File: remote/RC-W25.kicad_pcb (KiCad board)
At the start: 2 copper layers, 36 x 100.1 mm, 56 parts, among them J1 USB_C_Receptacle_USB2.0_14P, P1 JST CONN, P2 JST CONN, Q1 NMOS, SW1 Button, SW2 Button, SW3 YTSPS-22E58LM, SW4 Button, U1 ESP32-C6-MINI-1, U2 MCP73831-5-OT, U3 AP62300Z6, U4 TMAG5253

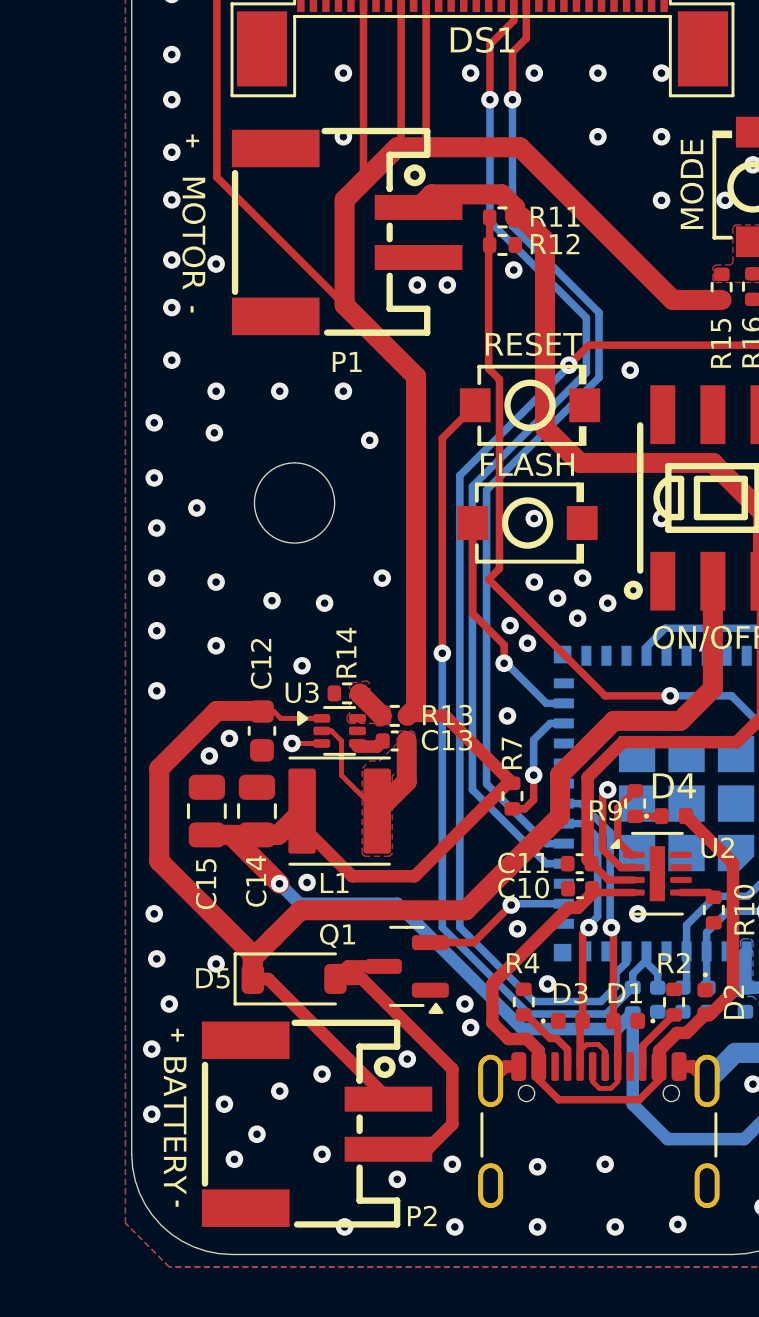
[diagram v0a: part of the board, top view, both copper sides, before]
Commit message: updated traces
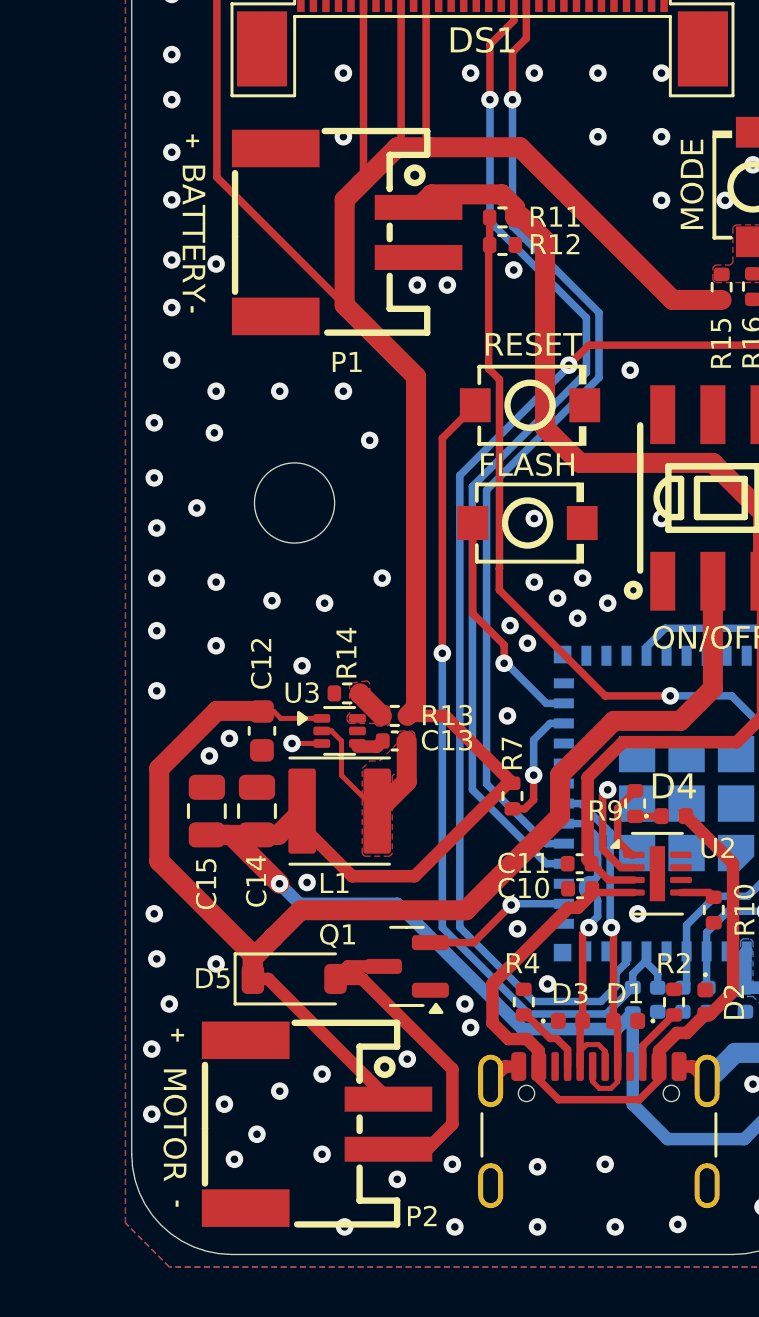
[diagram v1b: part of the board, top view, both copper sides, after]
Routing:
- net USB_D-: track 13.4 -> 14.2 mm
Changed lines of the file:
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@@
 		)
 	)
-	(gr_text "BATTERY"
+	(gr_text "MOTOR"
 		(at 112.7 119.8 270)
 		(layer "F.SilkS")
@@
 		)
 	)
-	(gr_text "MOTOR"
+	(gr_text "BATTERY"
 		(at 113.451866 84.206002 270)
 		(layer "F.SilkS")
@@
 	)
 	(segment
-		(start 129.9 102.7)
-		(end 125.25 98.05)
+		(start 125.675 97.625)
+		(end 125.68 97.62)
 		(width 0.3)
 		(layer "F.Cu")
@@
 	)
 	(segment
-		(start 132.5 102.7)
-		(end 129.9 102.7)
+		(start 125.25 84.74)
+		(end 125.29 84.7)
 		(width 0.3)
 		(layer "F.Cu")
@@
 	)
 	(segment
-		(start 125.25 84.74)
-		(end 125.29 84.7)
+		(start 125.68 90.07)
+		(end 125.25 89.64)
 		(width 0.3)
 		(layer "F.Cu")
@@
 	)
 	(segment
-		(start 125.68 90.07)
-		(end 125.25 89.64)
+		(start 125.68 97.62)
+		(end 125.68 90.07)
 		(width 0.3)
 		(layer "F.Cu")
@@
 	)
 	(segment
-		(start 125.25 98.05)
-		(end 125.68 97.62)
+		(start 132.5 102.7)
+		(end 129.9 102.7)
 		(width 0.3)
 		(layer "F.Cu")
@@
 	)
 	(segment
-		(start 125.68 97.62)
-		(end 125.68 90.07)
+		(start 129.9 102.7)
+		(end 125.675 98.475)
+		(width 0.3)
+		(layer "F.Cu")
+		(net 11)
+	)
+	(segment
+		(start 125.675 98.475)
+		(end 125.675 97.625)
 		(width 0.3)
 		(layer "F.Cu")
@@
 	)
 	(segment
-		(start 129.036093 107.8)
-		(end 128.25 107.8)
+		(start 129.25 111.949998)
+		(end 129.25 111.860051)
 		(width 0.3)
 		(layer "B.Cu")
@@
 	)
 	(segment
-		(start 129.25 111.949998)
-		(end 129.25 111.860051)
+		(start 129.36 110.654275)
+		(end 129.24 110.654275)
 		(width 0.3)
 		(layer "B.Cu")
@@
 	(segment
 		(start 129.6 111.510051)
-		(end 129.6 108.363907)
+		(end 129.6 110.894275)
+		(width 0.3)
+		(layer "B.Cu")
+		(net 19)
+	)
+	(segment
+		(start 129.036093 107.8)
+		(end 128.25 107.8)
 		(width 0.3)
 		(layer "B.Cu")
@@
 	)
 	(segment
+		(start 129.6 109.694275)
+		(end 129.6 109.553248)
+		(width 0.3)
+		(layer "B.Cu")
+		(net 19)
+	)
+	(segment
+		(start 129.6 109.553248)
+		(end 129.6 108.363907)
+		(width 0.3)
+		(layer "B.Cu")
+		(net 19)
+	)
+	(segment
+		(start 129.24 110.054275)
+		(end 129.36 110.054275)
+		(width 0.3)
+		(layer "B.Cu")
+		(net 19)
+	)
+	(segment
+		(start 129.6 109.814275)
+		(end 129.6 109.694275)
+		(width 0.3)
+		(layer "B.Cu")
+		(net 19)
+	)
+	(segment
+		(start 129 110.414275)
+		(end 129 110.294275)
+		(width 0.3)
+		(layer "B.Cu")
+		(net 19)
+	)
+	(arc
+		(start 129.36 110.054275)
+		(mid 129.529706 109.983981)
+		(end 129.6 109.814275)
+		(width 0.3)
+		(layer "B.Cu")
+		(net 19)
+	)
+	(arc
+		(start 129 110.294275)
+		(mid 129.070294 110.124569)
+		(end 129.24 110.054275)
+		(width 0.3)
+		(layer "B.Cu")
+		(net 19)
+	)
+	(arc
+		(start 129.6 110.894275)
+		(mid 129.529706 110.724569)
+		(end 129.36 110.654275)
+		(width 0.3)
+		(layer "B.Cu")
+		(net 19)
+	)
+	(arc
+		(start 129.24 110.654275)
+		(mid 129.070294 110.583981)
+		(end 129 110.414275)
+		(width 0.3)
+		(layer "B.Cu")
+		(net 19)
+	)
+	(segment
 		(start 132.14 107.51)
 		(end 132.15 107.5)
@@
 		)
 	)
+	(generated
+		(type tuning_pattern)
+		(name "Tuning Pattern")
+		(layer "B.Cu")
+		(base_line
+			(pts
+				(xy 129.6 110.894275) (xy 129.6 109.553248)
+			)
+		)
+		(corner_radius_percent 80)
+		(end
+			(xy 129.6 109.553248)
+		)
+		(initial_side "left")
+		(last_diff_pair_gap 0.18)
+		(last_netname "USB_D-")
+		(last_status "tuned")
+		(last_track_width 0.3)
+		(last_tuning "11.4774 mm (tuned)")
+		(max_amplitude 1)
+		(min_amplitude 0.2)
+		(min_spacing 0.6)
+		(origin
+			(xy 129.6 110.894275)
+		)
+		(override_custom_rules no)
+		(rounded yes)
+		(single_sided no)
+		(target_length 1000000)
+		(target_length_max 1000000)
+		(target_length_min 0)
+		(target_skew 0)
+		(target_skew_max 0.1)
+		(target_skew_min -0.1)
+		(tuning_mode "single")
+		(members "17cc8b51-adf3-4e6e-9451-abfa4a674d56" "2a80a1e3-7b09-4555-9cd4-e5b55d2daa5a"
+			"307ab3b6-0398-461d-9a12-6d7128e14987" "71b74942-a42e-4466-ac9a-01aa8737ae8c"
+			"856c1569-1c46-41f8-8312-75d96f11e951" "a7aceae7-cda2-42e2-861a-2e21ca846b52"
+			"bebe22a4-1710-4036-9746-54e66e6d4b58" "c35c4a82-8555-4b38-9e99-cf264392ba8c"
+			"dc328dce-c958-4ce4-8d3c-416cb03f53c3"
+		)
+	)

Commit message: CRC V3
V 3.0.0
Initial version of CRC V3, fully redesigned remote
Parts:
- removed G***: LOGO, LOGO
- removed H3: MountingHole, MountingHole:MountingHole_3.2mm_M3
- removed P1, P2: JST CONN, footprints:CONN-SMD_2P-P2.00_XUNPU_WAFER-PH2.0-2PWB
- removed SW1, SW2, SW4: Button, footprints:SW-SMD_L3.9-W3.0-P4.45
- removed SW3: YTSPS-22E58LM, footprints:SW-SMD_6P-YTSPS-22E58LM
- removed U4: TMAG5253, footprints:X2SON4_DMR_TEX
- added +3.3V: TEST POINT, TestPoint:TestPoint_Pad_2.0x2.0mm, F.Cu at (102.4, 126.1)
- added +USB5V: TEST POINT, TestPoint:TestPoint_Pad_2.0x2.0mm, F.Cu at (125.7, 129.5)
- added +VBAT: TEST POINT, TestPoint:TestPoint_Pad_2.0x2.0mm, F.Cu at (116.8, 122.0)
- added BATTERY: JST CONN, footprints:CONN-SMD_2P-P2.00_XUNPU_WAFER-PH2.0-2PWB, B.Cu at (120.6, 124.2)
- added BOOT: Button, footprints:SW-SMD_L3.9-W3.0-P4.45, F.Cu at (104.9, 100.5)
- added C18: 10uF, Capacitor_SMD:C_0402_1005Metric_Pad0.74x0.62mm_HandSolder, F.Cu at (121.0, 116.8)
- added C19: 100nF, Capacitor_SMD:C_0402_1005Metric_Pad0.74x0.62mm_HandSolder, F.Cu at (108.9, 121.0)
- added C20: 100nF, Capacitor_SMD:C_0402_1005Metric_Pad0.74x0.62mm_HandSolder, F.Cu at (107.9, 121.0)
- added D6: GLED, Diode_SMD:D_0402_1005Metric_Pad0.77x0.64mm_HandSolder, F.Cu at (105.7, 105.6)
- added D7: ZENER 5V, Diode_SMD:D_0402_1005Metric_Pad0.77x0.64mm_HandSolder, F.Cu at (118.9, 120.0)
- added D8: D_Schottky, Diode_SMD:D_SOD-123, F.Cu at (104.3, 93.5)
- added FB: TEST POINT, TestPoint:TestPoint_Pad_2.0x2.0mm, F.Cu at (113.5, 133.6)
- added JOYSTICK: TEST POINT, TestPoint:TestPoint_Pad_2.0x2.0mm, B.Cu at (114.6, 88.2)
- added JOYSTICK: JOYSTICK, footprints:Joystick Potentiometer Pads, B.Cu at (114.6, 84.0)
- added MODE: Button, footprints:Box Tactile Button Switch, F.Cu at (123.0, 102.0)
- added MOTOR: TEST POINT, TestPoint:TestPoint_Pad_2.0x2.0mm, F.Cu at (103.3, 90.2)
- added MOTOR: MOTOR, footprints:Motor Pads, B.Cu at (104.0, 91.5)
- added ON/OFF: Button, footprints:Box Tactile Button Switch, F.Cu at (123.0, 94.2)
- added R17: 1k, Resistor_SMD:R_0402_1005Metric_Pad0.72x0.64mm_HandSolder, F.Cu at (116.8, 119.2)
- added R18: 3.7k, Resistor_SMD:R_0402_1005Metric_Pad0.72x0.64mm_HandSolder, F.Cu at (116.8, 116.9)
- added R19: 1M, Resistor_SMD:R_0402_1005Metric_Pad0.72x0.64mm_HandSolder, F.Cu at (102.4, 123.8)
- added R20: 10k, Resistor_SMD:R_0402_1005Metric_Pad0.72x0.64mm_HandSolder, F.Cu at (117.6, 101.6)
- added R21: 10k, Resistor_SMD:R_0402_1005Metric_Pad0.72x0.64mm_HandSolder, F.Cu at (117.7, 93.8)
- added R22: 10k, Resistor_SMD:R_0402_1005Metric_Pad0.72x0.64mm_HandSolder, F.Cu at (118.2, 103.3)
- added R23: 10k, Resistor_SMD:R_0402_1005Metric_Pad0.72x0.64mm_HandSolder, F.Cu at (118.3, 95.5)
- added RESET: Button, footprints:SW-SMD_L3.9-W3.0-P4.45, F.Cu at (104.9, 96.7)
- added SCL: TEST POINT, TestPoint:TestPoint_Pad_2.0x2.0mm, F.Cu at (116.1, 91.0)
- added SDA: TEST POINT, TestPoint:TestPoint_Pad_2.0x2.0mm, F.Cu at (113.1, 91.0)
- C1: value 2.2uF -> 4.7uF; footprint Capacitor_SMD:C_0402_1005Metric -> Capacitor_SMD:C_0402_1005Metric_Pad0.74x0.62mm_HandSolder
- C10, C3, C4: footprint Capacitor_SMD:C_0402_1005Metric -> Capacitor_SMD:C_0402_1005Metric_Pad0.74x0.62mm_HandSolder
- C11: value 4.7uF -> 10uF; footprint Capacitor_SMD:C_0402_1005Metric -> Capacitor_SMD:C_0603_1608Metric_Pad1.08x0.95mm_HandSolder
- C12: footprint Capacitor_SMD:C_0603_1608Metric -> Capacitor_SMD:C_0603_1608Metric_Pad1.08x0.95mm_HandSolder
- C13: footprint Capacitor_SMD:C_0402_1005Metric -> Capacitor_SMD:C_0603_1608Metric_Pad1.08x0.95mm_HandSolder
- C14: value 22uF -> 1uF; footprint Capacitor_SMD:C_0805_2012Metric -> Capacitor_SMD:C_0402_1005Metric_Pad0.74x0.62mm_HandSolder
- C15: footprint Capacitor_SMD:C_0805_2012Metric -> Capacitor_SMD:C_0603_1608Metric_Pad1.08x0.95mm_HandSolder
- C16, C17: value 100nF -> 22uF; footprint Capacitor_SMD:C_0402_1005Metric -> Capacitor_SMD:C_0603_1608Metric_Pad1.08x0.95mm_HandSolder
- C2: value 2.2uF -> 10uF; footprint Capacitor_SMD:C_0402_1005Metric -> Capacitor_SMD:C_0402_1005Metric_Pad0.74x0.62mm_HandSolder
- C5, C6, C7, C9: footprint Capacitor_SMD:C_0402_1005Metric -> Capacitor_SMD:C_0402_1005Metric_Pad0.74x0.62mm_HandSolder; moved to F.Cu
- C8: footprint Capacitor_SMD:C_0805_2012Metric -> Capacitor_SMD:C_0805_2012Metric_Pad1.18x1.45mm_HandSolder; moved to F.Cu
- D1, D2, D3: footprint footprints:D_0402_1005Metric -> Diode_SMD:D_0402_1005Metric_Pad0.77x0.64mm_HandSolder
- D4: value LED -> RLED; footprint footprints:D_0402_1005Metric -> Diode_SMD:D_0402_1005Metric_Pad0.77x0.64mm_HandSolder
- D5: value D_Schottky -> ORLED; footprint Diode_SMD:D_SOD-123 -> Diode_SMD:D_0402_1005Metric_Pad0.77x0.64mm_HandSolder
- DS1: value FPC 0.5mm 30P -> FPC 0.7mm 30P; footprint footprints:FPC-30P-0.5mm -> footprints:FPC 0.7mm 30P
- L1: value 3.3uH -> 1.5uH
- R1: value 4.7k -> 390k; footprint Resistor_SMD:R_0402_1005Metric -> Resistor_SMD:R_0603_1608Metric_Pad0.98x0.95mm_HandSolder
- R10: value 2k -> 300; footprint Resistor_SMD:R_0402_1005Metric -> Resistor_SMD:R_0402_1005Metric_Pad0.72x0.64mm_HandSolder
- R11, R3, R7: footprint Resistor_SMD:R_0402_1005Metric -> Resistor_SMD:R_0402_1005Metric_Pad0.72x0.64mm_HandSolder
- R12: value 1.1k -> 5k; footprint Resistor_SMD:R_0402_1005Metric -> Resistor_SMD:R_0402_1005Metric_Pad0.72x0.64mm_HandSolder
- R13: value 31.6k -> 1k; footprint Resistor_SMD:R_0402_1005Metric -> Resistor_SMD:R_0402_1005Metric_Pad0.72x0.64mm_HandSolder
- R14: value 10k -> 1k; footprint Resistor_SMD:R_0402_1005Metric -> Resistor_SMD:R_0402_1005Metric_Pad0.72x0.64mm_HandSolder
- R15: value 10k -> 1M; footprint Resistor_SMD:R_0402_1005Metric -> Resistor_SMD:R_0402_1005Metric_Pad0.72x0.64mm_HandSolder
- R16: value 10k -> 180k; footprint Resistor_SMD:R_0402_1005Metric -> Resistor_SMD:R_0402_1005Metric_Pad0.72x0.64mm_HandSolder
- R2, R4: value 5.1k -> 4.7k; footprint Resistor_SMD:R_0402_1005Metric -> Resistor_SMD:R_0402_1005Metric_Pad0.72x0.64mm_HandSolder
- R5: value 390k -> 5.1k; footprint Resistor_SMD:R_0603_1608Metric -> Resistor_SMD:R_0402_1005Metric_Pad0.72x0.64mm_HandSolder
- R6: value 4.7k -> 5.1k; footprint Resistor_SMD:R_0402_1005Metric -> Resistor_SMD:R_0402_1005Metric_Pad0.72x0.64mm_HandSolder
- R8: footprint Resistor_SMD:R_0402_1005Metric -> Resistor_SMD:R_0402_1005Metric_Pad0.72x0.64mm_HandSolder; moved to F.Cu
- R9: value 470 -> 300; footprint Resistor_SMD:R_0402_1005Metric -> Resistor_SMD:R_0402_1005Metric_Pad0.72x0.64mm_HandSolder
- U1: moved to F.Cu
- U2: value MCP73831-5-OT -> BQ25185; footprint Package_DFN_QFN:DFN-8-1EP_2x3mm_P0.5mm_EP0.61x2.2mm -> footprints:WSON-10 BQ25185
- U3: value AP62300Z6 -> TPS63020; footprint Package_TO_SOT_SMD:SOT-563 -> footprints:TPS63020_VSON(14)
- moved H2 105.8 mm to (104.0, 136.0)
- moved C16 94.0 mm to (112.9, 129.0), turned to 90 degrees
- moved H1 81.8 mm to (123.0, 111.0)
- moved R6 59.9 mm to (117.2, 129.3), turned to 90 degrees
- moved R5 59.8 mm to (123.5, 129.3)
- moved R16 51.8 mm to (111.3, 132.0)
- moved R15 49.9 mm to (113.1, 131.4), turned to 180 degrees
- moved C17 48.2 mm to (114.5, 129.0)
- moved C8 35.5 mm to (102.0, 121.0), turned to 180 degrees
- moved R12 35.1 mm to (125.5, 119.8)
- moved C9 34.0 mm to (102.4, 122.6), turned to 180 degrees
- moved C11 33.9 mm to (101.6, 129.5), turned to 90 degrees
- moved R2 33.8 mm to (114.8, 86.2), turned to 0 degrees
- moved R10 31.9 mm to (103.1, 104.3), turned to 180 degrees
- moved R11 31.6 mm to (103.1, 105.6)
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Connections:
- net ADC_HALLEFFECT1 renamed ADC_JOYSTICK
- C1 pad 1: Net-(DS1-VDisplay) -> Net-(DS1-VCOMH)
- C11 pad 1: Net-(P1-Pin_1) -> +VSYS
- C12 pad 1: +VBAT -> +VSYS
- C13 pad 1: Net-(U3-SW) -> Net-(U3-PS/SYNC)
- C13 pad 2: Net-(U3-BST) -> GND
- C14 pad 1: +3.3V -> +VBAT
- C17 pad 1: GPIO_MODE -> +3.3V
- C2 pad 1: Net-(DS1-VCOMH) -> Net-(DS1-VDisplay)
- C6 pad 1: /RC_Connections/RESET -> ADC_BATTERYPERCENT
- C7 pad 1: ADC_BATTERYPERCENT -> /Connections/RESET
- D4 pad 2: +USB5V -> Net-(D4-A)
- D5 pad 1: +VBAT -> Net-(D5-K)
- DS1 pad 20: unconnected-(DS1-D2-Pad20) -> SCL_DISPLAY
- DS1 pad 7: GND -> unconnected-(DS1-N.C.-Pad7)
- L1 pad 1: Net-(U3-SW) -> Net-(L1-Pad1)
- L1 pad 2: +3.3V -> Net-(L1-Pad2)
- Q1 pad 3: Net-(D5-A) -> Net-(D8-A)
- R1 pad 1: +3.3V -> Net-(DS1-IREF)
- R1 pad 2: Net-(DS1-Reset) -> GND
- R10 pad 1: Net-(U2-PROG) -> Net-(D5-K)
- R11 pad 1: Net-(P1-Pin_1) -> Net-(D6-K)
- R11 pad 2: ADC_BATTERYPERCENT -> GND
- R12 pad 1: ADC_BATTERYPERCENT -> /Power/ILIM/VSET
- R13 pad 1: +3.3V -> Net-(U2-ISET)
- R13 pad 2: Net-(U3-FB) -> GND
- R14 pad 1: Net-(U3-FB) -> +3.3V
- R14 pad 2: GND -> /Power/TS/MR
- R15 pad 2: Net-(R15-Pad2) -> Net-(U3-FB)
- R16 pad 1: Net-(R15-Pad2) -> Net-(U3-FB)
- R16 pad 2: GPIO_MODE -> GND
- R2 pad 1: Net-(J1-CC2) -> +3.3V
- R2 pad 2: GND -> SDA_DISPLAY
- R3 pad 2: SDA_DISPLAY -> Net-(DS1-Reset)
- R4 pad 1: Net-(J1-CC1) -> +3.3V
- R4 pad 2: GND -> SCL_DISPLAY
- R5 pad 1: Net-(DS1-IREF) -> Net-(J1-CC2)
- R6 pad 1: +3.3V -> Net-(J1-CC1)
- R6 pad 2: SCL_DISPLAY -> GND
- R8 pad 2: /RC_Connections/RESET -> /Connections/RESET
- R9 pad 2: Net-(U2-STAT) -> GND
- U1 pad 10: unconnected-(U1-IO5-Pad10) -> GPIO_MODE
- U1 pad 15: SDA_DISPLAY -> CH_EN
- U1 pad 16: SCL_DISPLAY -> CHSTAT2
- U1 pad 23: /RC_Connections/FLASH -> /Connections/FLASH
- U1 pad 24: unconnected-(U1-IO18-Pad24) -> CHSTAT1
- U1 pad 25: unconnected-(U1-IO19-Pad25) -> SCL_DISPLAY
- U1 pad 26: unconnected-(U1-IO20-Pad26) -> SDA_DISPLAY
- U1 pad 27: unconnected-(U1-IO21-Pad27) -> Net-(D4-A)
- U1 pad 28: GPIO_EN1 -> Net-(D5-A)
- U1 pad 29: unconnected-(U1-IO23-Pad29) -> Net-(D6-A)
- U1 pad 8: /RC_Connections/RESET -> /Connections/RESET
- U1 pad 9: GPIO_MODE -> ON/OFF
- U2 pad 1: Net-(U2-STAT) -> +VSYS
- U2 pad 2: GND -> +VBAT
- U2 pad 3: Net-(P1-Pin_1) -> CHSTAT2
- U2 pad 4: +USB5V -> CH_EN
- U2 pad 5: Net-(U2-PROG) -> GND
- U2 pad 6: (no net) -> /Power/TS/MR
- U2 pad 7: (no net) -> /Power/ILIM/VSET
- U2 pad 8: (no net) -> Net-(U2-ISET)
- U2 pad 9: (no net) -> CHSTAT1
- U3 pad 1: +VBAT -> Net-(U3-PS/SYNC)
- U3 pad 2: Net-(U3-SW) -> GND
- U3 pad 3: GND -> Net-(U3-FB)
- U3 pad 4: Net-(U3-BST) -> +3.3V
- U3 pad 5: unconnected-(U3-EN-Pad5) -> +3.3V
- U3 pad 6: Net-(U3-FB) -> Net-(L1-Pad2)
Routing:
- net GPIO_EN1: track 72.4 -> 0.00 mm, vias 1 -> 0
- net Net-(P1-Pin_1): track 45.4 -> 0.00 mm
- net ADC_JOYSTICK: track 81.9 -> 42.3 mm
- net +VBAT: track 54.2 -> 16.7 mm, vias 0 -> 1
- net +VSYS: track 0.00 -> 34.4 mm, vias 0 -> 2
- net /RC_Connections/RESET: track 34.2 -> 0.00 mm, vias 1 -> 0
- net ON/OFF: track 0.00 -> 28.7 mm, vias 0 -> 2
- net GPIO_RUMBLE_CNTL: track 5.97 -> 33.0 mm, vias 1 -> 2
- net +3.3V: track 193.8 -> 167.0 mm, vias 1 -> 8
- net /Connections/RESET: track 0.00 -> 26.2 mm, vias 0 -> 2
- net ADC_BATTERYPERCENT: track 40.8 -> 15.3 mm, vias 1 -> 2
- net GPIO_MODE: track 45.0 -> 24.1 mm, vias 1 -> 2
- net CHSTAT1: track 0.00 -> 20.1 mm, vias 0 -> 2
- net SDA_DISPLAY: track 44.6 -> 26.8 mm, vias 1 -> 2
- net Net-(U3-PG): track 0.00 -> 13.8 mm, vias 0 -> 2
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- added copper zone on F.Cu, net +3.3V
- added copper zone on F.Cu, net +VSYS
- added copper zone on F.Cu, net Net-(L1-Pad1)
- added copper zone on F.Cu, net Net-(L1-Pad2)
- removed copper zone on B.Cu, net +3.3V
- removed copper zone on F.Cu, net Net-(R15-Pad2)
- removed copper zone on F.Cu, net Net-(U3-SW)
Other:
- board size 36 x 100.1 mm -> 27.4 x 60 mm
- board text removed: "+"
- board text removed: "-"
- board text removed: "BATTERY"
- board text removed: "FLASH"
- board text removed: "MATTHEW EMBAYE"
- board text removed: "MODE"
- board text removed: "MOTOR"
- board text removed: "OLED"
- board text removed: "ON/OFF"
- board text removed: "RESET"

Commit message: RCW25
Finalized for order
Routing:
- net +USB5V: track 25.3 -> 31.6 mm
- net +3.3V: track 167.0 -> 167.8 mm
- net GND: vias 110 -> 109

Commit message: Finalized design for review and order
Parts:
- added G***: LOGO, LOGO, B.Cu at (102.1, 112.1)
- DS1: value FPC 0.7mm 30P -> FPC 30P; footprint footprints:FPC 0.7mm 30P -> footprints:FPC-30P-0.5mm
- moved C2 18.5 mm to (104.3, 87.4)
- moved C3 17.3 mm to (121.5, 86.5), turned to 180 degrees
- moved C1 16.5 mm to (105.3, 87.4)
- moved R1 13.0 mm to (107.5, 87.8), turned to 180 degrees
- moved C4 12.8 mm to (119.3, 86.5), turned to 180 degrees
- moved R4 6.76 mm to (110.8, 87.1), turned to 0 degrees
- moved SCL 5.30 mm to (110.8, 90.9)
- moved R3 2.86 mm to (115.4, 87.1), turned to 180 degrees
- moved R2 1.92 mm to (113.1, 87.1), turned to 180 degrees
- moved DS1 1.20 mm to (113.7, 84.5), turned to 180 degrees
- moved SDA 0.81 mm to (113.9, 90.9)
- renumbered +USB5V to +USBV
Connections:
- U1 pad 25: SCL_DISPLAY -> SDA_DISPLAY
- U1 pad 26: SDA_DISPLAY -> SCL_DISPLAY
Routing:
- net SCL_DISPLAY: track 29.6 -> 24.4 mm
- net GND: track 3.22 -> 6.95 mm, vias 109 -> 107
- net +3.3V: track 167.8 -> 171.1 mm
- net GPIO_RUMBLE_CNTL: track 33.0 -> 30.6 mm
- net Net-(DS1-VDisplay): track 2.68 -> 4.58 mm
- net Net-(DS1-VCOMH): track 2.55 -> 4.18 mm
- net SDA_DISPLAY: track 26.8 -> 25.6 mm
- net Net-(DS1-C1N): track 2.88 -> 2.07 mm
- net Net-(DS1-C1P): track 2.70 -> 2.19 mm
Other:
- board text added: "MATTHEW EMBAYE"
